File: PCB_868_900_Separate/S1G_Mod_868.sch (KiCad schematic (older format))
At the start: 59 parts, among them Q1 DMG2307L-7, SW1 CUS-12TB, T1 0732511150, T2 0732511150, U1 AP7361-33FGE-7, U2 ADF7023BCPZ, X1 ABS05-32.768KHZ-9-T, X2 ABM11-140-26.000MHZ-T3

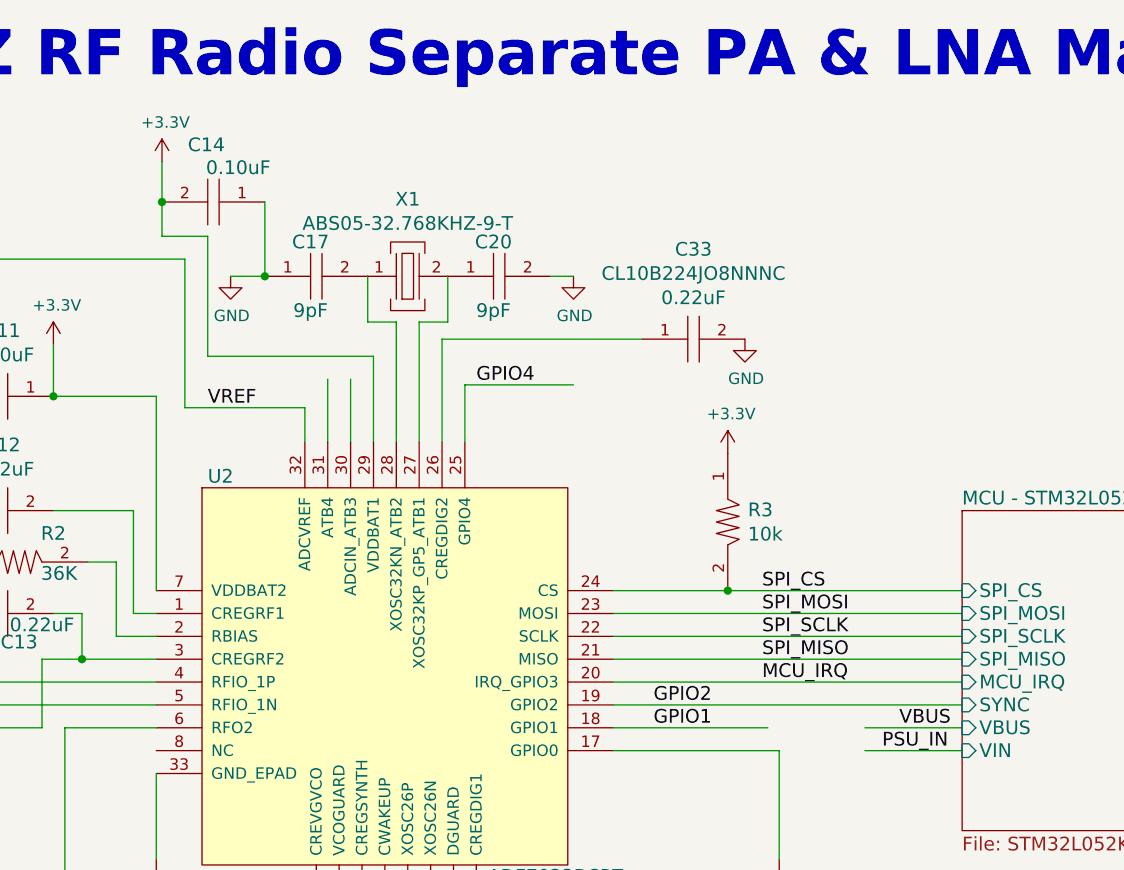
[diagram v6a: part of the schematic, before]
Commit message: SPI Resistors
Added 100 ohm inline resistors with SPI line and IRQ signal between
ADF7023 and STM32L0 on the separate antenna implementation.
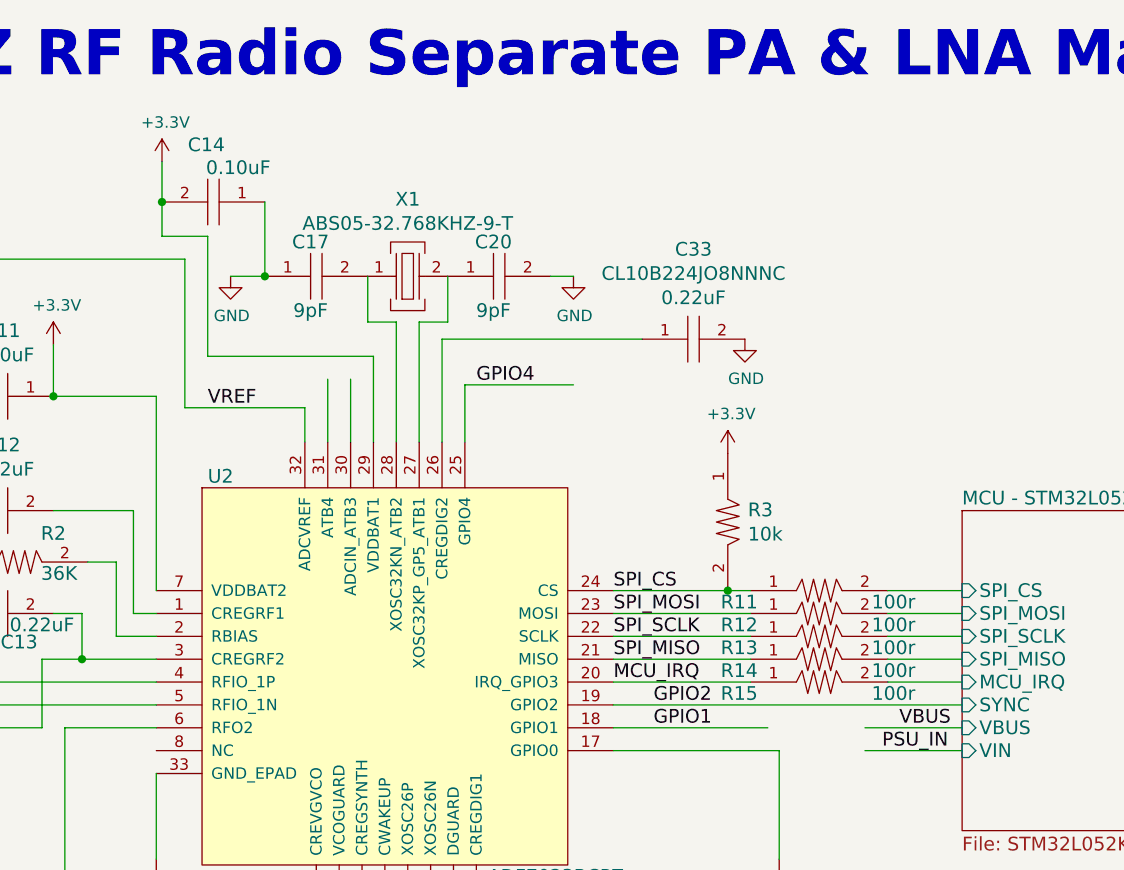
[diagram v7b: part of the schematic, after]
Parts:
- added R11, R12, R13, R14, R15: TNPW0402100RBEED, PCB_Footprints:R0402, symbol TNPW0402100RBEED
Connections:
- wire segments 93 -> 98
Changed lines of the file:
@@
 Text Label 4475 6900 0    60   ~ 0
 ON_OFF
-Text Label 8500 3200 0    60   ~ 0
+Text Label 7850 3200 0    60   ~ 0
 SPI_CS
-Text Label 8500 3300 0    60   ~ 0
+Text Label 7850 3300 0    60   ~ 0
 SPI_MOSI
-Text Label 8500 3400 0    60   ~ 0
+Text Label 7850 3400 0    60   ~ 0
 SPI_SCLK
-Text Label 8500 3500 0    60   ~ 0
+Text Label 7850 3500 0    60   ~ 0
 SPI_MISO
-Text Label 8500 3600 0    60   ~ 0
+Text Label 7850 3600 0    60   ~ 0
 MCU_IRQ
 $Comp
@@
 Connection ~ 5400 2350
 Wire Wire Line
-	7850 3200 9375 3200
-Wire Wire Line
-	9375 3300 7850 3300
-Wire Wire Line
-	7850 3400 9375 3400
-Wire Wire Line
-	9375 3500 7850 3500
-Wire Wire Line
-	7850 3600 9375 3600
+	7850 3200 8450 3200
+Wire Wire Line
+	8450 3300 7850 3300
+Wire Wire Line
+	7850 3400 8450 3400
+Wire Wire Line
+	8450 3500 7850 3500
+Wire Wire Line
+	7850 3600 8450 3600
 Connection ~ 2000 4600
 Connection ~ 2800 4600
@@
 	6075 2175 6075 1650
 Wire Wire Line
-	6075 1650 5875 1650
+	5875 1650 6075 1650
 Wire Wire Line
 	6775 1825 6775 2025
@@
 	7850 3800 8525 3800
 Wire Wire Line
-	5875 1650 5875 1325
+	5875 1325 5875 1650
 Connection ~ 5875 1500
 Wire Wire Line
@@
 NoConn ~ 9100 5100
 NoConn ~ 9100 5575
+$Comp
+L TNPW0402100RBEED R11
+U 1 1 582BE80F
+P 8750 3200
+F 0 "R11" H 8400 3150 60  0000 C CNN
+F 1 "TNPW0402100RBEED" H 8750 3447 60  0001 C CNN
+F 2 "PCB_Footprints:R0402" H 8350 3450 60  0001 C CNN
+F 3 "http://www.vishay.com/docs/28758/tnpw_e3.pdf" H 8450 3650 60  0001 C CNN
+F 4 "0.11880 @ 2500" H 10300 5150 60  0001 C CNN "Cost"
+F 5 "14 Nov 2016" H 8650 3750 60  0001 C CNN "Date Created"
+F 6 "14 Nov 2016" H 8750 3850 60  0001 C CNN "Date Modified"
+F 7 "Adam Vadala-Roth" H 8850 3950 60  0001 C CNN "Designer"
+F 8 "0.4mm" H 8950 4050 60  0001 C CNN "Height"
+F 9 "Yes" H 9050 4150 60  0001 C CNN "RHoS?"
+F 10 "Vishay Dale" H 9150 4250 60  0001 C CNN "MFR"
+F 11 "TNPW0402100RBEED" H 9250 4350 60  0001 C CNN "MFR#"
+F 12 "SMT/SMD" H 9350 4450 60  0001 C CNN "Mounting"
+F 13 "2" H 9450 4550 60  0001 C CNN "Pin Count#"
+F 14 "Active" H 9550 4650 60  0001 C CNN "Status"
+F 15 "0.1%" H 9650 4750 60  0001 C CNN "Tolerance"
+F 16 "passive" H 9750 4850 60  0001 C CNN "Type"
+F 17 "N/A" H 9850 4950 60  0001 C CNN "Voltage"
+F 18 "1/16" H 9950 5050 60  0001 C CNN "Wattage"
+F 19 "100r" H 9075 3150 60  0000 C CNN "Component-Value"
+F 20 "RES SMD 100 OHM 0.1% 1/16W 0402" H 10150 5250 60  0001 C CNN "Description"
+	1    8750 3200
+	1    0    0    -1
+$EndComp
+$Comp
+L TNPW0402100RBEED R12
+U 1 1 582C2492
+P 8750 3300
+F 0 "R12" H 8400 3250 60  0000 C CNN
+F 1 "TNPW0402100RBEED" H 8750 3547 60  0001 C CNN
+F 2 "PCB_Footprints:R0402" H 8350 3550 60  0001 C CNN
+F 3 "http://www.vishay.com/docs/28758/tnpw_e3.pdf" H 8450 3750 60  0001 C CNN
+F 4 "0.11880 @ 2500" H 10300 5250 60  0001 C CNN "Cost"
+F 5 "14 Nov 2016" H 8650 3850 60  0001 C CNN "Date Created"
+F 6 "14 Nov 2016" H 8750 3950 60  0001 C CNN "Date Modified"
+F 7 "Adam Vadala-Roth" H 8850 4050 60  0001 C CNN "Designer"
+F 8 "0.4mm" H 8950 4150 60  0001 C CNN "Height"
+F 9 "Yes" H 9050 4250 60  0001 C CNN "RHoS?"
+F 10 "Vishay Dale" H 9150 4350 60  0001 C CNN "MFR"
+F 11 "TNPW0402100RBEED" H 9250 4450 60  0001 C CNN "MFR#"
+F 12 "SMT/SMD" H 9350 4550 60  0001 C CNN "Mounting"
+F 13 "2" H 9450 4650 60  0001 C CNN "Pin Count#"
+F 14 "Active" H 9550 4750 60  0001 C CNN "Status"
+F 15 "0.1%" H 9650 4850 60  0001 C CNN "Tolerance"
+F 16 "passive" H 9750 4950 60  0001 C CNN "Type"
+F 17 "N/A" H 9850 5050 60  0001 C CNN "Voltage"
+F 18 "1/16" H 9950 5150 60  0001 C CNN "Wattage"
+F 19 "100r" H 9075 3250 60  0000 C CNN "Component-Value"
+F 20 "RES SMD 100 OHM 0.1% 1/16W 0402" H 10150 5350 60  0001 C CNN "Description"
+	1    8750 3300
+	1    0    0    -1
+$EndComp
+$Comp
+L TNPW0402100RBEED R13
+U 1 1 582C25B3
+P 8750 3400
+F 0 "R13" H 8400 3350 60  0000 C CNN
+F 1 "TNPW0402100RBEED" H 8750 3647 60  0001 C CNN
+F 2 "PCB_Footprints:R0402" H 8350 3650 60  0001 C CNN
+F 3 "http://www.vishay.com/docs/28758/tnpw_e3.pdf" H 8450 3850 60  0001 C CNN
+F 4 "0.11880 @ 2500" H 10300 5350 60  0001 C CNN "Cost"
+F 5 "14 Nov 2016" H 8650 3950 60  0001 C CNN "Date Created"
+F 6 "14 Nov 2016" H 8750 4050 60  0001 C CNN "Date Modified"
+F 7 "Adam Vadala-Roth" H 8850 4150 60  0001 C CNN "Designer"
+F 8 "0.4mm" H 8950 4250 60  0001 C CNN "Height"
+F 9 "Yes" H 9050 4350 60  0001 C CNN "RHoS?"
+F 10 "Vishay Dale" H 9150 4450 60  0001 C CNN "MFR"
+F 11 "TNPW0402100RBEED" H 9250 4550 60  0001 C CNN "MFR#"
+F 12 "SMT/SMD" H 9350 4650 60  0001 C CNN "Mounting"
+F 13 "2" H 9450 4750 60  0001 C CNN "Pin Count#"
+F 14 "Active" H 9550 4850 60  0001 C CNN "Status"
+F 15 "0.1%" H 9650 4950 60  0001 C CNN "Tolerance"
+F 16 "passive" H 9750 5050 60  0001 C CNN "Type"
+F 17 "N/A" H 9850 5150 60  0001 C CNN "Voltage"
+F 18 "1/16" H 9950 5250 60  0001 C CNN "Wattage"
+F 19 "100r" H 9075 3350 60  0000 C CNN "Component-Value"
+F 20 "RES SMD 100 OHM 0.1% 1/16W 0402" H 10150 5450 60  0001 C CNN "Description"
+	1    8750 3400
+	1    0    0    -1
+$EndComp
+$Comp
+L TNPW0402100RBEED R14
+U 1 1 582C26D3
+P 8750 3500
+F 0 "R14" H 8400 3450 60  0000 C CNN
+F 1 "TNPW0402100RBEED" H 8750 3747 60  0001 C CNN
+F 2 "PCB_Footprints:R0402" H 8350 3750 60  0001 C CNN
+F 3 "http://www.vishay.com/docs/28758/tnpw_e3.pdf" H 8450 3950 60  0001 C CNN
+F 4 "0.11880 @ 2500" H 10300 5450 60  0001 C CNN "Cost"
+F 5 "14 Nov 2016" H 8650 4050 60  0001 C CNN "Date Created"
+F 6 "14 Nov 2016" H 8750 4150 60  0001 C CNN "Date Modified"
+F 7 "Adam Vadala-Roth" H 8850 4250 60  0001 C CNN "Designer"
+F 8 "0.4mm" H 8950 4350 60  0001 C CNN "Height"
+F 9 "Yes" H 9050 4450 60  0001 C CNN "RHoS?"
+F 10 "Vishay Dale" H 9150 4550 60  0001 C CNN "MFR"
+F 11 "TNPW0402100RBEED" H 9250 4650 60  0001 C CNN "MFR#"
+F 12 "SMT/SMD" H 9350 4750 60  0001 C CNN "Mounting"
+F 13 "2" H 9450 4850 60  0001 C CNN "Pin Count#"
+F 14 "Active" H 9550 4950 60  0001 C CNN "Status"
+F 15 "0.1%" H 9650 5050 60  0001 C CNN "Tolerance"
+F 16 "passive" H 9750 5150 60  0001 C CNN "Type"
+F 17 "N/A" H 9850 5250 60  0001 C CNN "Voltage"
+F 18 "1/16" H 9950 5350 60  0001 C CNN "Wattage"
+F 19 "100r" H 9075 3450 60  0000 C CNN "Component-Value"
+F 20 "RES SMD 100 OHM 0.1% 1/16W 0402" H 10150 5550 60  0001 C CNN "Description"
+	1    8750 3500
+	1    0    0    -1
+$EndComp
+Wire Wire Line
+	9050 3200 9375 3200
+Wire Wire Line
+	9050 3300 9375 3300
+Wire Wire Line
+	9375 3400 9050 3400
+Wire Wire Line
+	9375 3500 9050 3500
+$Comp
+L TNPW0402100RBEED R15
+U 1 1 582C41A3
+P 8750 3600
+F 0 "R15" H 8400 3550 60  0000 C CNN
+F 1 "TNPW0402100RBEED" H 8750 3847 60  0001 C CNN
+F 2 "PCB_Footprints:R0402" H 8350 3850 60  0001 C CNN
+F 3 "http://www.vishay.com/docs/28758/tnpw_e3.pdf" H 8450 4050 60  0001 C CNN
+F 4 "0.11880 @ 2500" H 10300 5550 60  0001 C CNN "Cost"
+F 5 "14 Nov 2016" H 8650 4150 60  0001 C CNN "Date Created"
+F 6 "14 Nov 2016" H 8750 4250 60  0001 C CNN "Date Modified"
+F 7 "Adam Vadala-Roth" H 8850 4350 60  0001 C CNN "Designer"
+F 8 "0.4mm" H 8950 4450 60  0001 C CNN "Height"
+F 9 "Yes" H 9050 4550 60  0001 C CNN "RHoS?"
+F 10 "Vishay Dale" H 9150 4650 60  0001 C CNN "MFR"
+F 11 "TNPW0402100RBEED" H 9250 4750 60  0001 C CNN "MFR#"
+F 12 "SMT/SMD" H 9350 4850 60  0001 C CNN "Mounting"
+F 13 "2" H 9450 4950 60  0001 C CNN "Pin Count#"
+F 14 "Active" H 9550 5050 60  0001 C CNN "Status"
+F 15 "0.1%" H 9650 5150 60  0001 C CNN "Tolerance"
+F 16 "passive" H 9750 5250 60  0001 C CNN "Type"
+F 17 "N/A" H 9850 5350 60  0001 C CNN "Voltage"
+F 18 "1/16" H 9950 5450 60  0001 C CNN "Wattage"
+F 19 "100r" H 9075 3550 60  0000 C CNN "Component-Value"
+F 20 "RES SMD 100 OHM 0.1% 1/16W 0402" H 10150 5650 60  0001 C CNN "Description"
+	1    8750 3600
+	1    0    0    -1
+$EndComp
+Wire Wire Line
+	9375 3600 9050 3600
 $EndSCHEMATC

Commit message: USB VDD
Found schematic bug, USB VDD was not tied to 3V3 supply or applied a
bypass cap, this has been resolved in both implementations of the S1G.
STM32L0 program manual added to the datasheets collection for the
project. Schematic PDFs updated.
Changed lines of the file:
@@
 $EndComp
 $Comp
-L GND #PWR26
+L GND #PWR01
 U 1 1 58161058
 P 7000 6125
-F 0 "#PWR26" H 7000 5875 50  0001 C CNN
+F 0 "#PWR01" H 7000 5875 50  0001 C CNN
 F 1 "GND" H 7005 5952 50  0000 C CNN
 F 2 "" H 7000 6125 50  0000 C CNN
@@
 $EndComp
 $Comp
-L GND #PWR18
+L GND #PWR02
 U 1 1 5816222C
 P 5850 4375
-F 0 "#PWR18" H 5850 4125 50  0001 C CNN
+F 0 "#PWR02" H 5850 4125 50  0001 C CNN
 F 1 "GND" H 5855 4202 50  0000 C CNN
 F 2 "" H 5850 4375 50  0000 C CNN
@@
 $EndComp
 $Comp
-L +3.3V #PWR17
+L +3.3V #PWR03
 U 1 1 581623E1
 P 5400 2125
-F 0 "#PWR17" H 5400 1975 50  0001 C CNN
+F 0 "#PWR03" H 5400 1975 50  0001 C CNN
 F 1 "+3.3V" H 5415 2298 50  0000 C CNN
 F 2 "" H 5400 2125 50  0000 C CNN
@@
 $EndComp
 $Comp
-L GND #PWR15
+L GND #PWR04
 U 1 1 58162F98
 P 4950 3300
-F 0 "#PWR15" H 4950 3050 50  0001 C CNN
+F 0 "#PWR04" H 4950 3050 50  0001 C CNN
 F 1 "GND" H 4955 3127 50  0000 C CNN
 F 2 "" H 4950 3300 50  0000 C CNN
@@
 $EndComp
 $Comp
-L GND #PWR24
+L GND #PWR05
 U 1 1 58164E94
 P 6200 5050
-F 0 "#PWR24" H 6200 4800 50  0001 C CNN
+F 0 "#PWR05" H 6200 4800 50  0001 C CNN
 F 1 "GND" H 6205 4877 50  0000 C CNN
 F 2 "" H 6200 5050 50  0000 C CNN
@@
 $EndComp
 $Comp
-L GND #PWR27
+L GND #PWR06
 U 1 1 58165059
 P 7250 5050
-F 0 "#PWR27" H 7250 4800 50  0001 C CNN
+F 0 "#PWR06" H 7250 4800 50  0001 C CNN
 F 1 "GND" H 7255 4877 50  0000 C CNN
 F 2 "" H 7250 5050 50  0000 C CNN
@@
 $EndComp
 $Comp
-L GND #PWR25
+L GND #PWR07
 U 1 1 58165567
 P 6850 5050
-F 0 "#PWR25" H 6850 4800 50  0001 C CNN
+F 0 "#PWR07" H 6850 4800 50  0001 C CNN
 F 1 "GND" H 6855 4877 50  0000 C CNN
 F 2 "" H 6850 5050 50  0000 C CNN
@@
 $EndComp
 $Comp
-L GND #PWR31
+L GND #PWR08
 U 1 1 58168376
 P 8575 5475
-F 0 "#PWR31" H 8575 5225 50  0001 C CNN
+F 0 "#PWR08" H 8575 5225 50  0001 C CNN
 F 1 "GND" H 8580 5302 50  0000 C CNN
 F 2 "" H 8575 5475 50  0000 C CNN
@@
 $EndComp
 $Comp
-L +3.3V #PWR19
+L +3.3V #PWR09
 U 1 1 58168986
 P 5875 1325
-F 0 "#PWR19" H 5875 1175 50  0001 C CNN
+F 0 "#PWR09" H 5875 1175 50  0001 C CNN
 F 1 "+3.3V" H 5890 1498 50  0000 C CNN
 F 2 "" H 5875 1325 50  0000 C CNN
@@
 $EndComp
 $Comp
-L GND #PWR14
+L GND #PWR010
 U 1 1 58169314
 P 4950 2350
-F 0 "#PWR14" H 4950 2100 50  0001 C CNN
+F 0 "#PWR010" H 4950 2100 50  0001 C CNN
 F 1 "GND" H 4955 2177 50  0000 C CNN
 F 2 "" H 4950 2350 50  0000 C CNN
@@
 $EndComp
 $Comp
-L GND #PWR2
+L GND #PWR011
 U 1 1 5817FFB1
 P 725 4875
-F 0 "#PWR2" H 725 4625 50  0001 C CNN
+F 0 "#PWR011" H 725 4625 50  0001 C CNN
 F 1 "GND" H 730 4702 50  0000 C CNN
 F 2 "" H 725 4875 50  0000 C CNN
@@
 $EndComp
 $Comp
-L GND #PWR3
+L GND #PWR012
 U 1 1 58174222
 P 2000 5050
-F 0 "#PWR3" H 2000 4800 50  0001 C CNN
+F 0 "#PWR012" H 2000 4800 50  0001 C CNN
 F 1 "GND" H 2005 4877 50  0000 C CNN
 F 2 "" H 2000 5050 50  0000 C CNN
@@
 $EndComp
 $Comp
-L GND #PWR5
+L GND #PWR013
 U 1 1 581744A7
 P 2800 5050
-F 0 "#PWR5" H 2800 4800 50  0001 C CNN
+F 0 "#PWR013" H 2800 4800 50  0001 C CNN
 F 1 "GND" H 2805 4877 50  0000 C CNN
 F 2 "" H 2800 5050 50  0000 C CNN
@@
 $EndComp
 $Comp
-L GND #PWR11
+L GND #PWR014
 U 1 1 5816BC64
 P 4000 6500
-F 0 "#PWR11" H 4000 6250 50  0001 C CNN
+F 0 "#PWR014" H 4000 6250 50  0001 C CNN
 F 1 "GND" H 4005 6327 50  0000 C CNN
 F 2 "" H 4000 6500 50  0000 C CNN
@@
 $EndComp
 $Comp
-L GND #PWR21
+L GND #PWR015
 U 1 1 5816BFC1
 P 5875 6500
-F 0 "#PWR21" H 5875 6250 50  0001 C CNN
+F 0 "#PWR015" H 5875 6250 50  0001 C CNN
 F 1 "GND" H 5880 6327 50  0000 C CNN
 F 2 "" H 5875 6500 50  0000 C CNN
@@
 $EndComp
 $Comp
-L +3.3V #PWR20
+L +3.3V #PWR016
 U 1 1 5816C55D
 P 5875 6050
-F 0 "#PWR20" H 5875 5900 50  0001 C CNN
+F 0 "#PWR016" H 5875 5900 50  0001 C CNN
 F 1 "+3.3V" H 5890 6223 50  0000 C CNN
 F 2 "" H 5875 6050 50  0000 C CNN
@@
 MCU_IRQ
 $Comp
-L GND #PWR23
+L GND #PWR017
 U 1 1 58175F58
 P 6175 1825
-F 0 "#PWR23" H 6175 1575 50  0001 C CNN
+F 0 "#PWR017" H 6175 1575 50  0001 C CNN
 F 1 "GND" H 6180 1652 50  0000 C CNN
 F 2 "" H 6175 1825 50  0000 C CNN
@@
 $EndComp
 $Comp
-L GND #PWR28
+L GND #PWR018
 U 1 1 581763CA
 P 7675 1825
-F 0 "#PWR28" H 7675 1575 50  0001 C CNN
+F 0 "#PWR018" H 7675 1575 50  0001 C CNN
 F 1 "GND" H 7680 1652 50  0000 C CNN
 F 2 "" H 7675 1825 50  0000 C CNN
@@
 $EndComp
 $Comp
-L GND #PWR9
+L GND #PWR019
 U 1 1 5817CEBD
 P 3650 2200
-F 0 "#PWR9" H 3650 1950 50  0001 C CNN
+F 0 "#PWR019" H 3650 1950 50  0001 C CNN
 F 1 "GND" H 3655 2027 50  0000 C CNN
 F 2 "" H 3650 2200 50  0000 C CNN
@@
 $EndComp
 $Comp
-L GND #PWR13
+L GND #PWR020
 U 1 1 5817CF2D
 P 4450 2200
-F 0 "#PWR13" H 4450 1950 50  0001 C CNN
+F 0 "#PWR020" H 4450 1950 50  0001 C CNN
 F 1 "GND" H 4455 2027 50  0000 C CNN
 F 2 "" H 4450 2200 50  0000 C CNN
@@
 $EndComp
 $Comp
-L +3.3V #PWR6
+L +3.3V #PWR021
 U 1 1 5817CF98
 P 3150 1750
-F 0 "#PWR6" H 3150 1600 50  0001 C CNN
+F 0 "#PWR021" H 3150 1600 50  0001 C CNN
 F 1 "+3.3V" H 3165 1923 50  0000 C CNN
 F 2 "" H 3150 1750 50  0000 C CNN
@@
 $EndComp
 $Comp
-L GND #PWR8
+L GND #PWR022
 U 1 1 5818E84F
 P 3600 5050
-F 0 "#PWR8" H 3600 4800 50  0001 C CNN
+F 0 "#PWR022" H 3600 4800 50  0001 C CNN
 F 1 "GND" H 3605 4877 50  0000 C CNN
 F 2 "" H 3600 5050 50  0000 C CNN
@@
 $EndComp
 $Comp
-L GND #PWR10
+L GND #PWR023
 U 1 1 58195E9E
 P 3675 4100
-F 0 "#PWR10" H 3675 3850 50  0001 C CNN
+F 0 "#PWR023" H 3675 3850 50  0001 C CNN
 F 1 "GND" H 3680 3927 50  0000 C CNN
 F 2 "" H 3675 4100 50  0000 C CNN
@@
 $EndComp
 $Comp
-L GND #PWR4
+L GND #PWR024
 U 1 1 58196935
 P 2800 3025
-F 0 "#PWR4" H 2800 2775 50  0001 C CNN
+F 0 "#PWR024" H 2800 2775 50  0001 C CNN
 F 1 "GND" H 2805 2852 50  0000 C CNN
 F 2 "" H 2800 3025 50  0000 C CNN
@@
 $EndComp
 $Comp
-L GND #PWR1
+L GND #PWR025
 U 1 1 581979F7
 P 700 3650
-F 0 "#PWR1" H 700 3400 50  0001 C CNN
+F 0 "#PWR025" H 700 3400 50  0001 C CNN
 F 1 "GND" H 705 3477 50  0000 C CNN
 F 2 "" H 700 3650 50  0000 C CNN
@@
 $EndComp
 $Comp
-L +3.3V #PWR29
+L +3.3V #PWR026
 U 1 1 581AA58C
 P 8350 2600
-F 0 "#PWR29" H 8350 2450 50  0001 C CNN
+F 0 "#PWR026" H 8350 2450 50  0001 C CNN
 F 1 "+3.3V" H 8365 2773 50  0000 C CNN
 F 2 "" H 8350 2600 50  0000 C CNN
@@
 	6075 2175 6075 1650
 Wire Wire Line
-	5875 1650 6075 1650
+	6075 1650 5875 1650
 Wire Wire Line
 	6775 1825 6775 2025
@@
 	7850 3800 8525 3800
 Wire Wire Line
-	5875 1325 5875 1650
+	5875 1650 5875 1325
 Connection ~ 5875 1500
 Wire Wire Line
@@
 	6175 7300 6450 7300
 $Comp
-L GND #PWR22
+L GND #PWR027
 U 1 1 5822EA21
 P 6050 7125
-F 0 "#PWR22" H 6050 6875 50  0001 C CNN
+F 0 "#PWR027" H 6050 6875 50  0001 C CNN
 F 1 "GND" H 6055 6952 50  0000 C CNN
 F 2 "" H 6050 7125 50  0000 C CNN
@@
 $EndComp
 $Comp
-L GND #PWR12
+L GND #PWR028
 U 1 1 5825B89E
 P 4150 5250
-F 0 "#PWR12" H 4150 5000 50  0001 C CNN
+F 0 "#PWR028" H 4150 5000 50  0001 C CNN
 F 1 "GND" H 4155 5077 50  0000 C CNN
 F 2 "" H 4150 5250 50  0000 C CNN
@@
 $EndComp
 $Comp
-L GND #PWR16
+L GND #PWR029
 U 1 1 582688A4
 P 4950 7350
-F 0 "#PWR16" H 4950 7100 50  0001 C CNN
+F 0 "#PWR029" H 4950 7100 50  0001 C CNN
 F 1 "GND" H 4955 7177 50  0000 C CNN
 F 2 "" H 4950 7350 50  0000 C CNN
@@
 	3850 7350 3425 7350
 $Comp
-L +3.3V #PWR7
+L +3.3V #PWR030
 U 1 1 582692EE
 P 3425 7350
-F 0 "#PWR7" H 3425 7200 50  0001 C CNN
+F 0 "#PWR030" H 3425 7200 50  0001 C CNN
 F 1 "+3.3V" H 3440 7523 50  0000 C CNN
 F 2 "" H 3425 7350 50  0000 C CNN
@@
 	7100 2100 7100 2550
 $Comp
-L GND #PWR30
+L GND #PWR031
 U 1 1 582AF362
 P 8425 2100
-F 0 "#PWR30" H 8425 1850 50  0001 C CNN
+F 0 "#PWR031" H 8425 1850 50  0001 C CNN
 F 1 "GND" H 8430 1927 50  0000 C CNN
 F 2 "" H 8425 2100 50  0000 C CNN
